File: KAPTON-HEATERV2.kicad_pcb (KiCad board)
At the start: 2 copper layers, 107 x 63.1 mm, 37 parts, among them J1 XT60PW-M, J2 XT60PW-M, J3 1985276, J4 1985218, J5 10090926-P154XLF, K1 1-1393210-8, Q1 AO3400A, U1 TC4427ACOA, U2 INA181

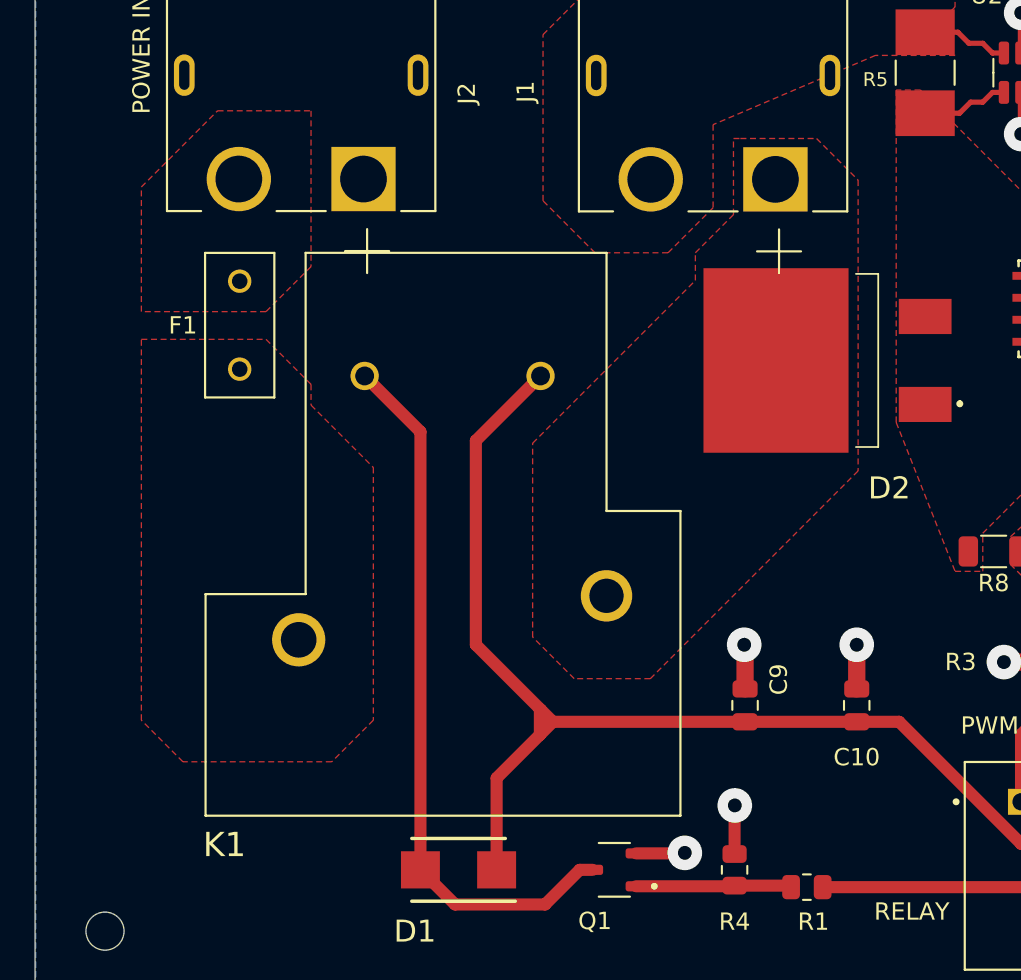
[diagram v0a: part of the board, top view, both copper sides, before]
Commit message: New Relay Footprint
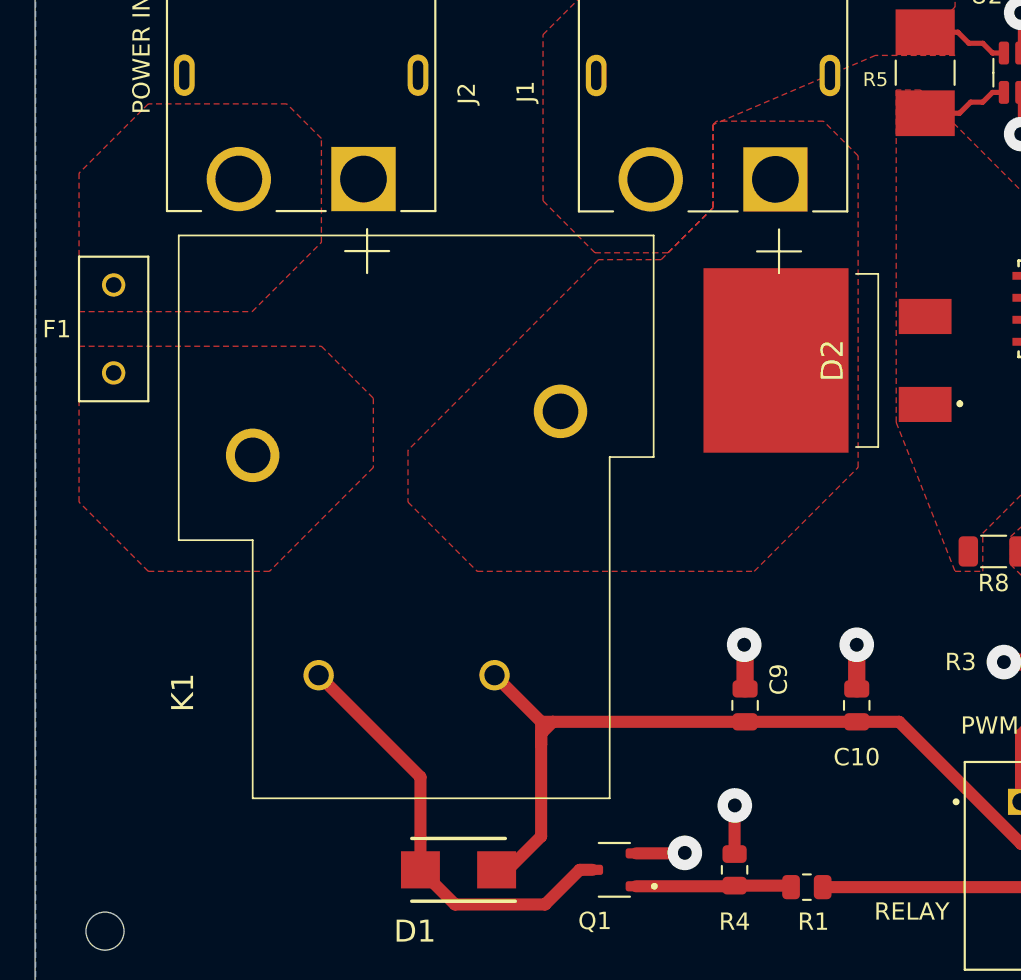
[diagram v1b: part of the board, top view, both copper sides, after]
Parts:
- K1: value 1-1393210-8 -> T9AS1D12-5; footprint T9AS1D12_24:RELAY_1-1393210-8 -> LIB_T9AS1D12-5:T9AS1D125
- moved K1 8.67 mm to (120.0, 114.0), turned to 0 degrees
- moved F1 7.28 mm to (98.0, 94.0)
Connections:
- J1 pad S1: GND -> (no net)
- J1 pad S2: GND -> (no net)
- J2 pad S1: GND -> (no net)
- J2 pad S2: GND -> (no net)
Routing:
- net 5V: track 169.9 -> 151.2 mm
- net Net-(D1-A): track 41.5 -> 25.3 mm
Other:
- board text added: "2-1393210-0"

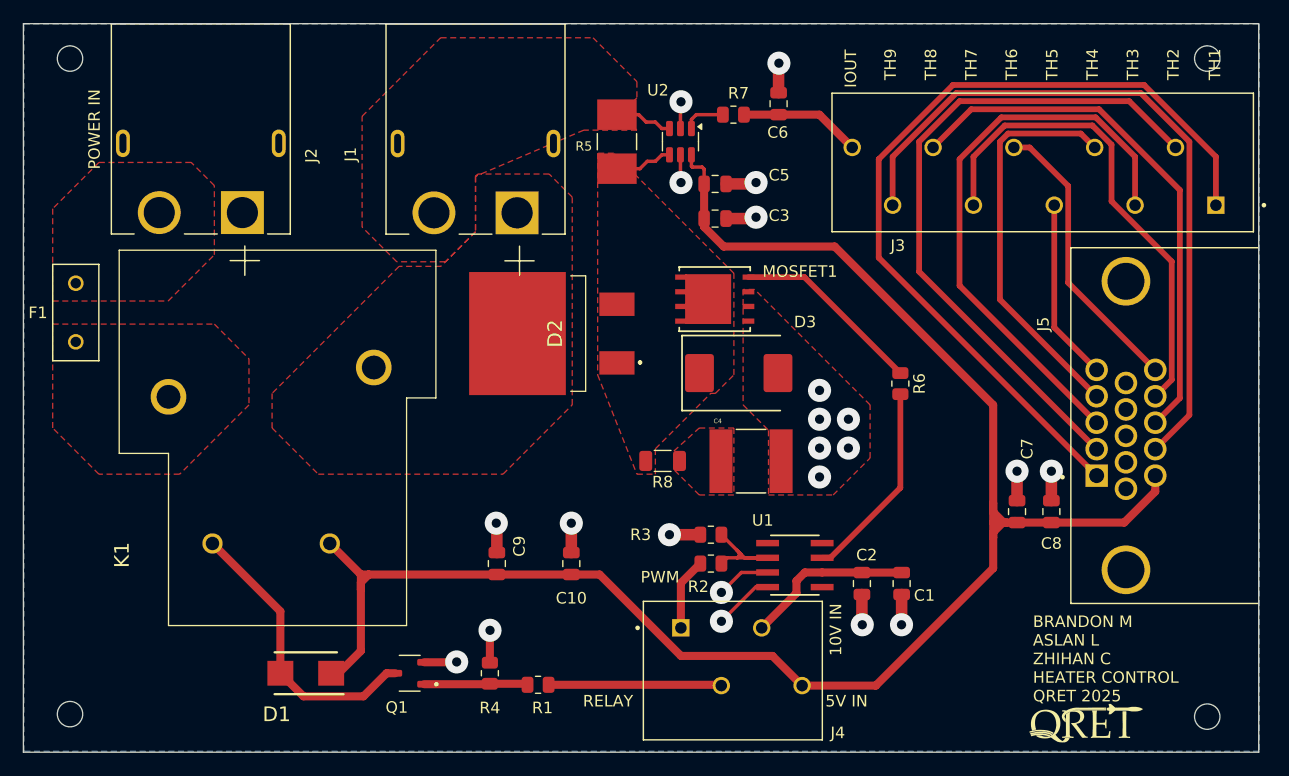
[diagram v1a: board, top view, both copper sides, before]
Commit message: Rounded to Nearest mm
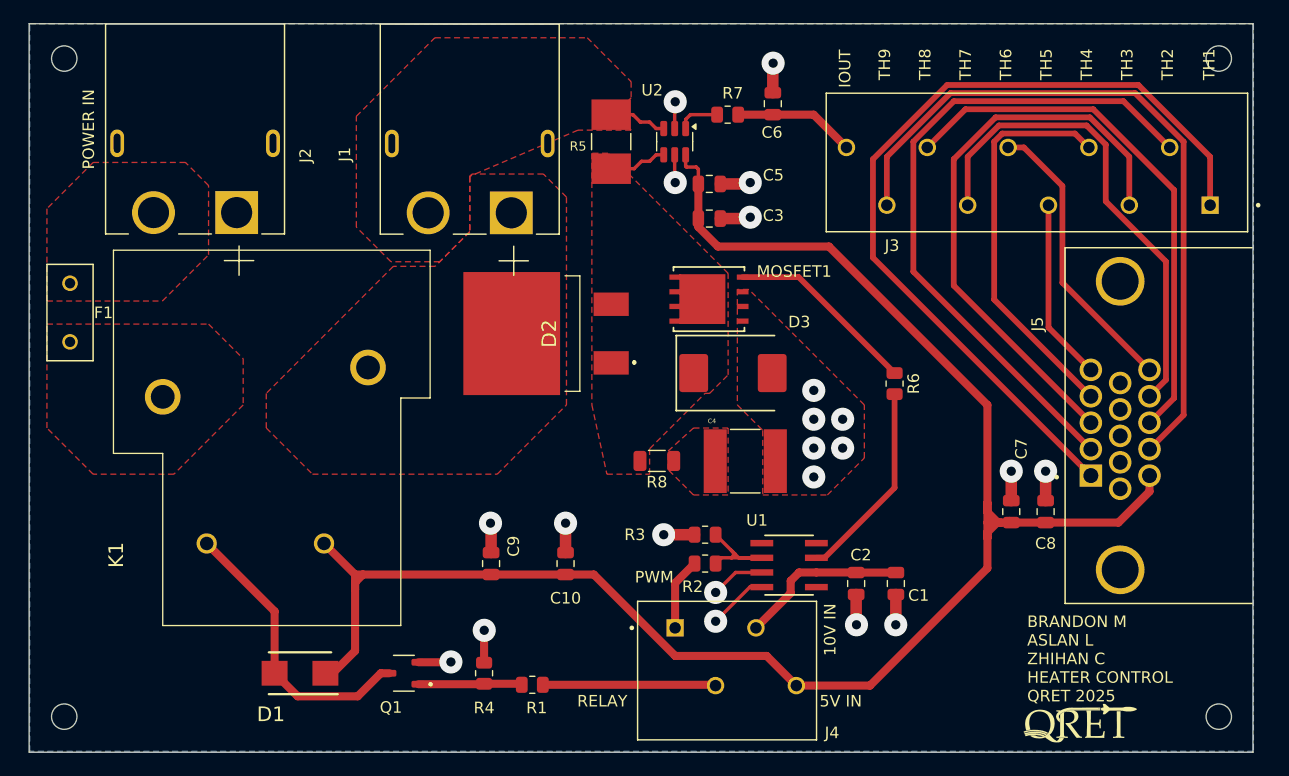
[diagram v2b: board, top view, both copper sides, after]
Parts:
- moved REF** 1.00 mm to (197.0, 129.0)
- moved REF** 1.00 mm to (197.0, 72.0)
- moved REF** 0.55 mm to (97.0, 129.0)
- moved C1 0.50 mm to (169.0, 117.5)
- moved C10 0.50 mm to (140.4, 115.7)
- moved C2 0.50 mm to (165.6, 117.5)
- moved C3 0.50 mm to (152.9, 85.9)
- moved C4 0.50 mm to (156.0, 106.9)
- moved C5 0.50 mm to (152.9, 82.9)
- moved C6 0.50 mm to (158.4, 75.9)
- moved C7 0.50 mm to (179.0, 111.2)
- moved C8 0.50 mm to (182.0, 111.2)
- moved C9 0.50 mm to (134.0, 115.7)
- moved D1 0.50 mm to (117.4, 125.2)
- moved D2 0.50 mm to (132.9, 95.8)
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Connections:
- J1 pad S1: (no net) -> GND
- J1 pad S2: (no net) -> GND
- J2 pad S1: (no net) -> GND
- J2 pad S2: (no net) -> GND
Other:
- board size 107 x 63.1 mm -> 106 x 63.1 mm

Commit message: Trace Edit and Gerbers
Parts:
- moved C10 2.42 mm to (138.0, 115.7)
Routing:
- net TH3: track 50.1 -> 38.1 mm
- net TH4: track 34.5 -> 26.2 mm
- net TH6: track 25.1 -> 32.4 mm
- net TH7: track 42.5 -> 44.0 mm
- net TH1: track 73.9 -> 75.1 mm
- net TH8: track 46.7 -> 47.7 mm
- net TH9: track 61.8 -> 62.7 mm
- net 5V: track 151.2 -> 151.9 mm
- net TH2: track 58.3 -> 59.0 mm
